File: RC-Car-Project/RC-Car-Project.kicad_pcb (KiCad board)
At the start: 2 copper layers, 80 x 120 mm, 130 parts, among them J1 Conn_01x02_Pin, J10 ANT_IF, J11 Conn_01x02, J2 Conn_01x02_Pin, J3 Conn_01x02_Pin, J4 Conn_01x02_Pin, J5 MCU_IF, J6 Conn_01x02, J7 Conn_01x02, J8 Conn_01x02, J9 Conn_02x09_Odd_Even, Q1 BTN8982TA, Q2 BTN8982TA, Q3 BTN8982TA, Q4 2N7002E, Q4 BTN8982TA, Q5 2N7002E, Q6 2N7002E, SW1 SW_Push, U1 LMR16020PDDAR, U10 2450LP14A0100001T, U2 A6986F3V3TR, U3 STM32H743VGTx, U4 AT86RF215-ZU, U5 2450FB15A050E, U6 RFX2401C, U7 INA229AQDGSRQ1, U8 ADC082S021CIMM/NOPB, U9 SN74HC244PWR, Y1 Crystal

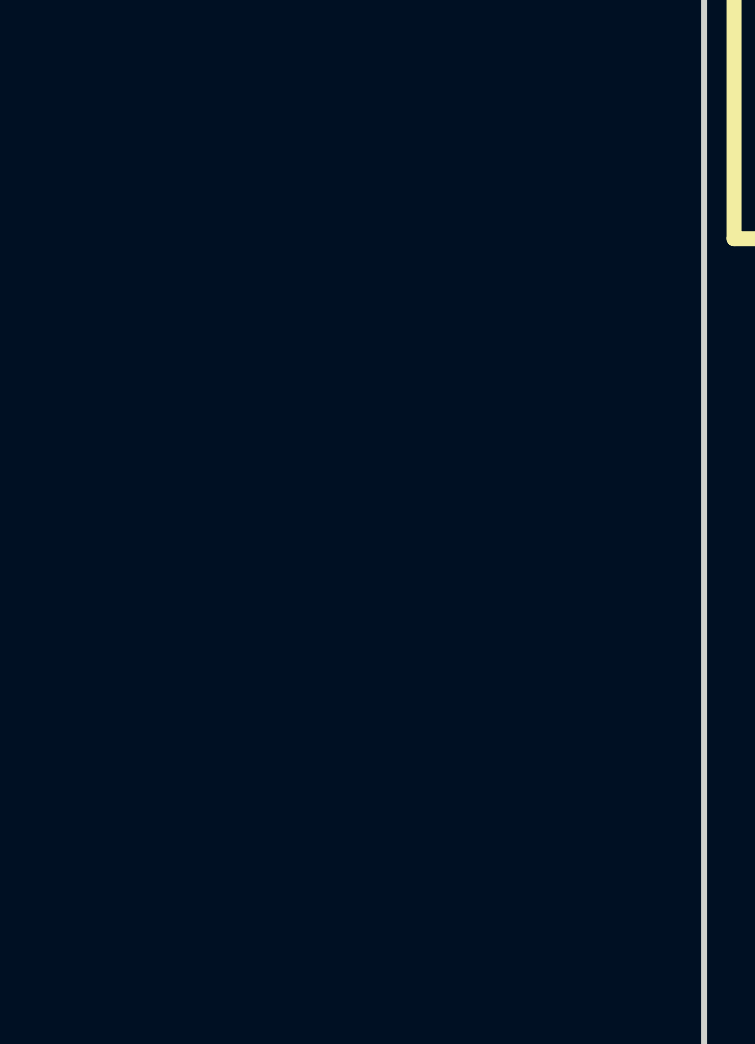
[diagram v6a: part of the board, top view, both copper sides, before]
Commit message: Fixed Borked Connectors
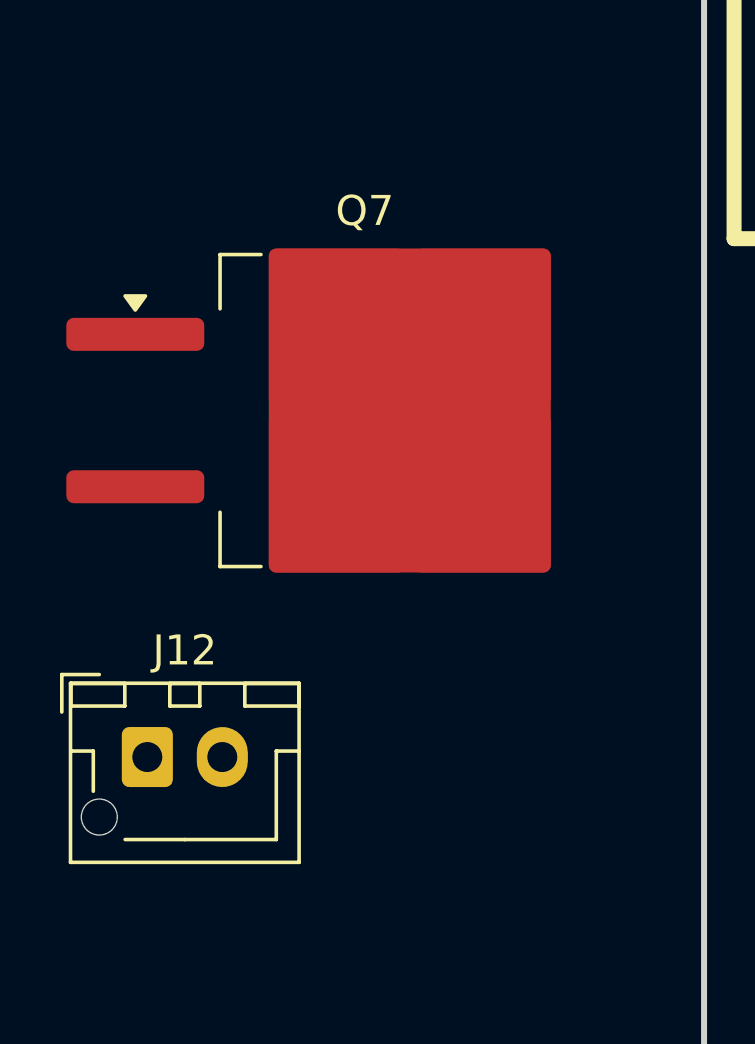
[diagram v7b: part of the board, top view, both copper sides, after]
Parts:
- added J12: Conn_01x02, Connector_JST:JST_XH_B2B-XH-AM_1x02_P2.50mm_Vertical, F.Cu at (91.4, 104.3)
- added Q7: PMOS, Package_TO_SOT_SMD:TO-263-2, F.Cu at (98.7, 92.7)

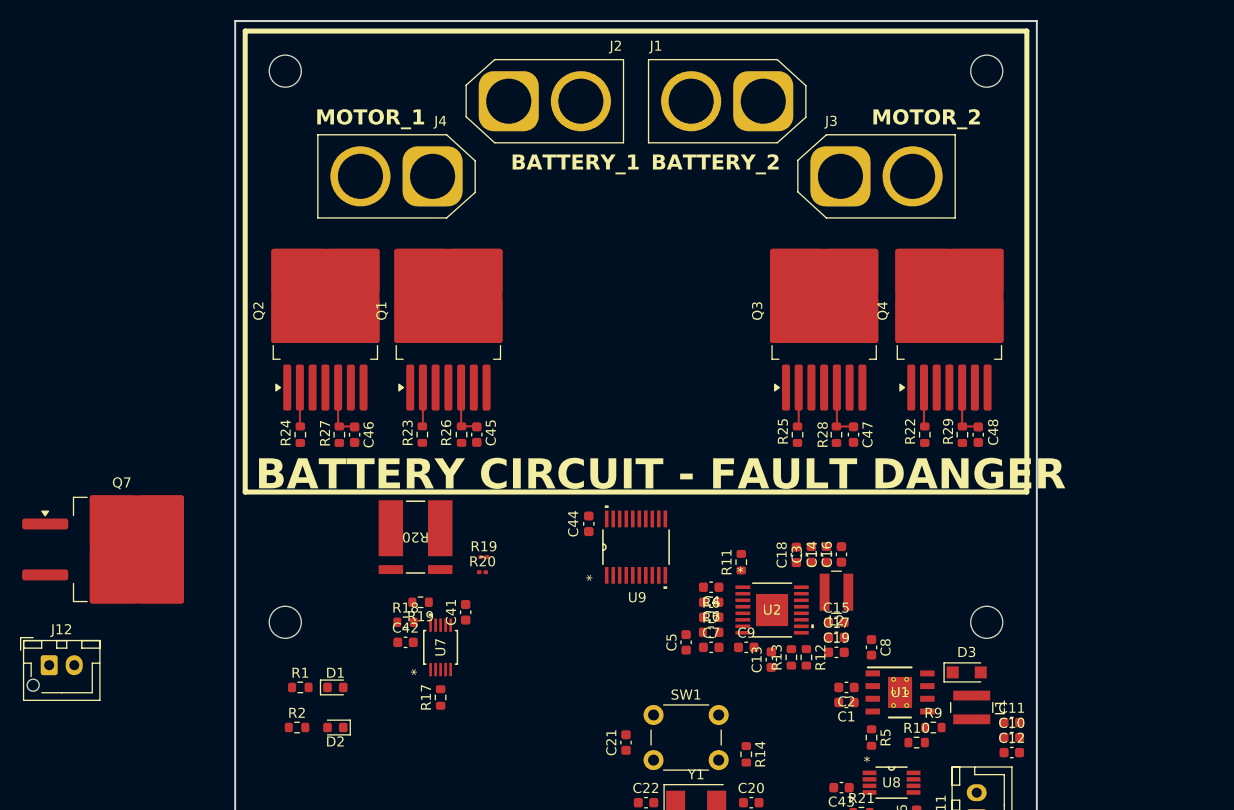
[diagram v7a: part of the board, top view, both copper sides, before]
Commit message: Add Bulk dcaps, layout HV sw, change mosfet footprint to TH
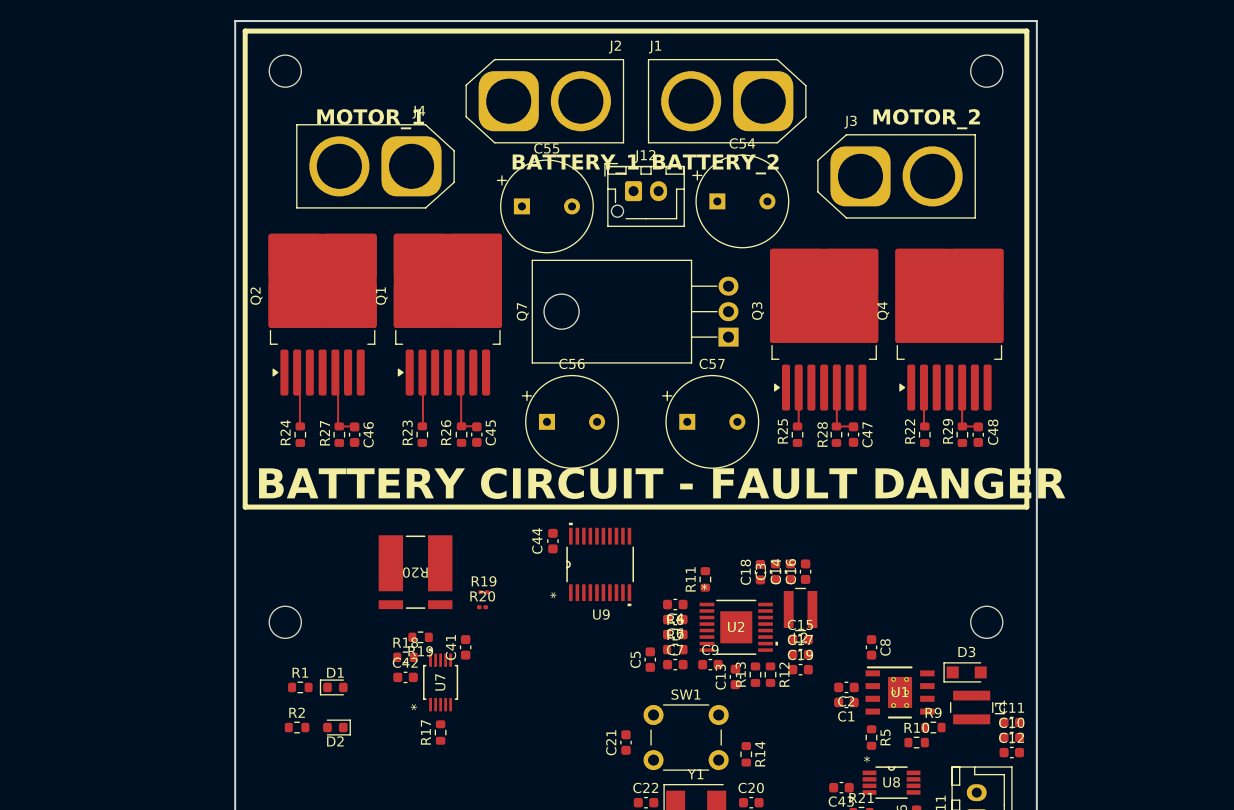
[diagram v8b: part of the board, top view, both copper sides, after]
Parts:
- added C54: C_Polarized, Capacitor_THT:CP_Radial_Tantal_D9.0mm_P5.00mm, F.Cu at (158.1, 58.0)
- added C55: C_Polarized, Capacitor_THT:CP_Radial_Tantal_D9.0mm_P5.00mm, F.Cu at (138.6, 58.5)
- added C56: C_Polarized, Capacitor_THT:CP_Radial_Tantal_D9.0mm_P5.00mm, F.Cu at (141.1, 80.0)
- added C57: C_Polarized, Capacitor_THT:CP_Radial_Tantal_D9.0mm_P5.00mm, F.Cu at (155.1, 80.0)
- Q7: footprint Package_TO_SOT_SMD:TO-263-2 -> Package_TO_SOT_THT:TO-220-3_Horizontal_TabDown
- moved J12 75.1 mm to (149.8, 57.0)
- moved Q7 64.1 mm to (159.2, 71.5), turned to 90 degrees
- moved C13 3.97 mm to (159.9, 105.5)
- moved C14 3.97 mm to (165.4, 95.0)
- moved C15 3.97 mm to (166.4, 101.7)
- moved C16 3.97 mm to (166.9, 95.0)
- moved C17 3.97 mm to (166.4, 103.2)
- moved C19 3.97 mm to (166.4, 104.7)
- moved C3 3.97 mm to (163.9, 95.0)
- moved C4 3.97 mm to (153.9, 98.2)
- moved C5 3.97 mm to (151.4, 103.7)
- moved C6 3.97 mm to (153.9, 99.7)
- moved C7 3.97 mm to (153.9, 104.2)
- moved C9 3.97 mm to (157.4, 104.2)
- moved L2 3.97 mm to (166.4, 98.7)
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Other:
- board text removed: "Batt Caps?"
